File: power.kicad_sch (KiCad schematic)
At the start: 18 parts, among them U2 BQ25176J, U3 TPS61201DRC

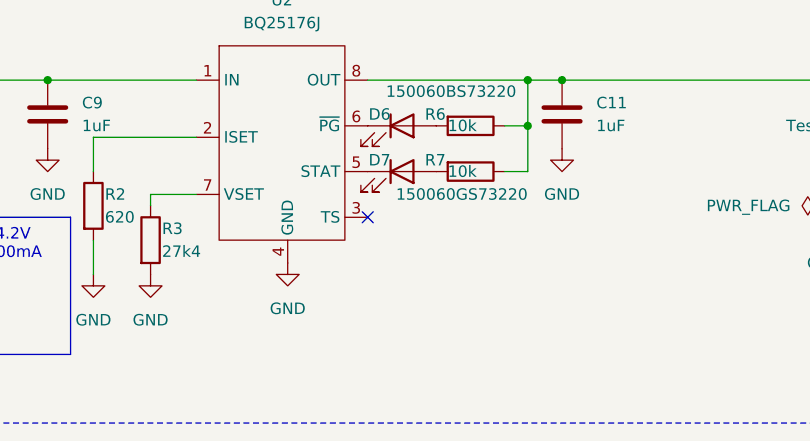
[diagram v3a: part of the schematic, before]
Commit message: fix battery charging IC circuit missing TS pulldown
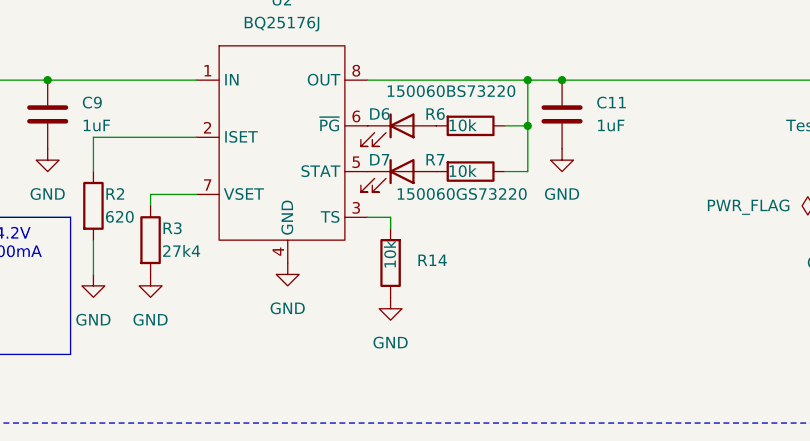
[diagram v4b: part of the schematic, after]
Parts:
- added R14: 10k, Resistor_SMD:R_0805_2012Metric, symbol Device:R
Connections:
- net GND: now also R14.1
- net at U2.3 (TS): now also R14.2
- no-connect marks 1 -> 0
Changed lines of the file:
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@@
 		(color 0 0 0 0)
 	)
-	(no_connect
-		(at 74.93 135.89)
-	)
 	(wire
 		(pts
@@
 	(wire
 		(pts
+			(xy 77.47 137.16) (xy 77.47 135.89)
+		)
+		(stroke
+			(width 0)
+			(type default)
+		)
+	)
+	(wire
+		(pts
 			(xy 68.58 57.15) (xy 80.01 57.15)
 		)
@@
 		(pts
 			(xy 60.96 57.15) (xy 68.58 57.15)
+		)
+		(stroke
+			(width 0)
+			(type default)
+		)
+	)
+	(wire
+		(pts
+			(xy 77.47 135.89) (xy 74.93 135.89)
 		)
 		(stroke
@@
 	)
 	(symbol
+		(lib_id "Device:R")
+		(at 77.47 140.97 180)
+		(unit 1)
+		(exclude_from_sim no)
+		(in_bom yes)
+		(on_board yes)
+		(dnp no)
+		(property "Reference" "R14"
+			(at 83.82 140.716 0)
+			(effects
+				(font
+					(size 1.27 1.27)
+				)
+				(justify left)
+			)
+		)
+		(property "Value" "10k"
+			(at 77.47 138.43 90)
+			(effects
+				(font
+					(size 1.27 1.27)
+				)
+				(justify left)
+			)
+		)
+		(property "Footprint" "Resistor_SMD:R_0805_2012Metric"
+			(at 79.248 140.97 90)
+			(effects
+				(font
+					(size 1.27 1.27)
+				)
+				(hide yes)
+			)
+		)
+		(property "Datasheet" "~"
+			(at 77.47 140.97 0)
+			(effects
+				(font
+					(size 1.27 1.27)
+				)
+				(hide yes)
+			)
+		)
+		(property "Description" "Resistor"
+			(at 77.47 140.97 0)
+			(effects
+				(font
+					(size 1.27 1.27)
+				)
+				(hide yes)
+			)
+		)
+		(property "mpn" "CR0805-FX-1002ELF "
+			(at 77.47 140.97 0)
+			(effects
+				(font
+					(size 1.27 1.27)
+				)
+				(hide yes)
+			)
+		)
+		(pin "1"
+		)
+		(pin "2"
+		)
+		(instances
+			(project "bierdeckel"
+				(path "/a4ffe097-37ef-4e19-a91a-ae57f4a5aad1/06d9cd17-cb19-4cdd-8e67-c41d1b4a676e"
+					(reference "R14")
+					(unit 1)
+				)
+			)
+		)
+	)
+	(symbol
 		(lib_id "power:+3.3V")
 		(at 125.73 59.69 0)
@@
 					(unit 1)
 				)
+			)
+		)
+	)
+	(symbol
+		(lib_id "power:GND")
+		(at 77.47 144.78 0)
+		(unit 1)
+		(exclude_from_sim no)
+		(in_bom yes)
+		(on_board yes)
+		(dnp no)
+		(fields_autoplaced yes)
+		(property "Reference" "#PWR010"
+			(at 77.47 151.13 0)
+			(effects
+				(font
+					(size 1.27 1.27)
+				)
+				(hide yes)
+			)
+		)
+		(property "Value" "GND"
+			(at 77.47 149.86 0)
+			(effects
+				(font
+					(size 1.27 1.27)
+				)
+			)
+		)
+		(property "Footprint" ""
+			(at 77.47 144.78 0)
+			(effects
+				(font
+					(size 1.27 1.27)
+				)
+				(hide yes)
+			)
+		)
+		(property "Datasheet" ""
+			(at 77.47 144.78 0)
+			(effects
+				(font
+					(size 1.27 1.27)
+				)
+				(hide yes)
+			)
+		)
+		(property "Description" "Power symbol creates a global label with name \"GND\" , ground"
+			(at 77.47 144.78 0)
+			(effects
+				(font
+					(size 1.27 1.27)
+				)
+				(hide yes)
+			)
+		)
+		(pin "1"
+		)
+		(instances
+			(project "bierdeckel"
+				(path "/a4ffe097-37ef-4e19-a91a-ae57f4a5aad1/06d9cd17-cb19-4cdd-8e67-c41d1b4a676e"
+					(reference "#PWR010")
+					(unit 1)
+				)

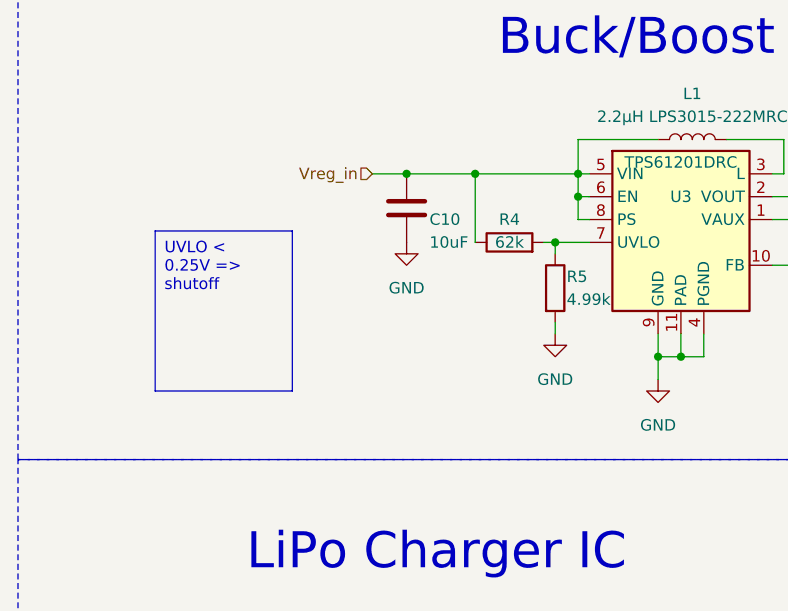
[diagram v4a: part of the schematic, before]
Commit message: correct buck/boost bootstrap circuit to handle falling/rising hysteresis on Uvlo
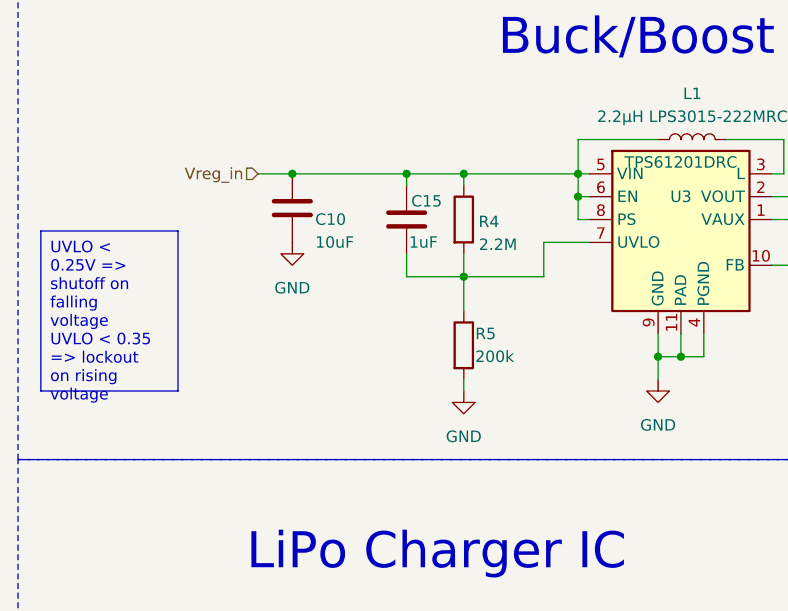
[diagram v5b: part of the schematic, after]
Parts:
- added C15: 1uF, Capacitor_SMD:C_0805_2012Metric, symbol Device:C
- R4: value 62k -> 2.2M
- R5: value 4.99k -> 200k
- U3: footprint Package_SON:Texas_S-PVSON-N10_ThermalVias -> bier:Texas_S-PVSON-N10_ThermalVias; symbol Regulator_Switching:TPS61201DRC -> bier:TPS61201DRC
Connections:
- net Vreg_in: now also C15.1
- net at R4.2, R5.1, U3.7 (UVLO): now also C15.2
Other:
- moved on the sheet: C10, R4, R5

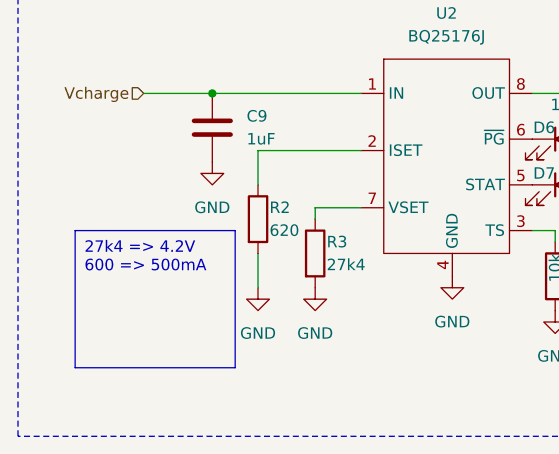
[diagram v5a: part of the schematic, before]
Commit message: change to 2 pressure gauge strips
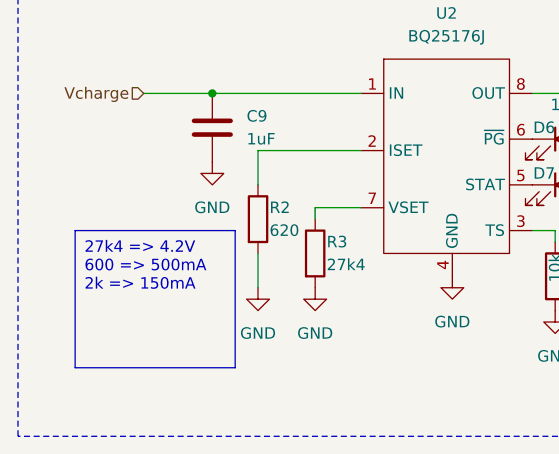
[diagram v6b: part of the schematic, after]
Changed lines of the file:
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@@
 		)
 	)
-	(text_box "27k4 => 4.2V\n600 => 500mA"
+	(text_box "27k4 => 4.2V\n600 => 500mA\n2k => 150mA"
 		(exclude_from_sim no)
 		(at 24.13 135.89 0)

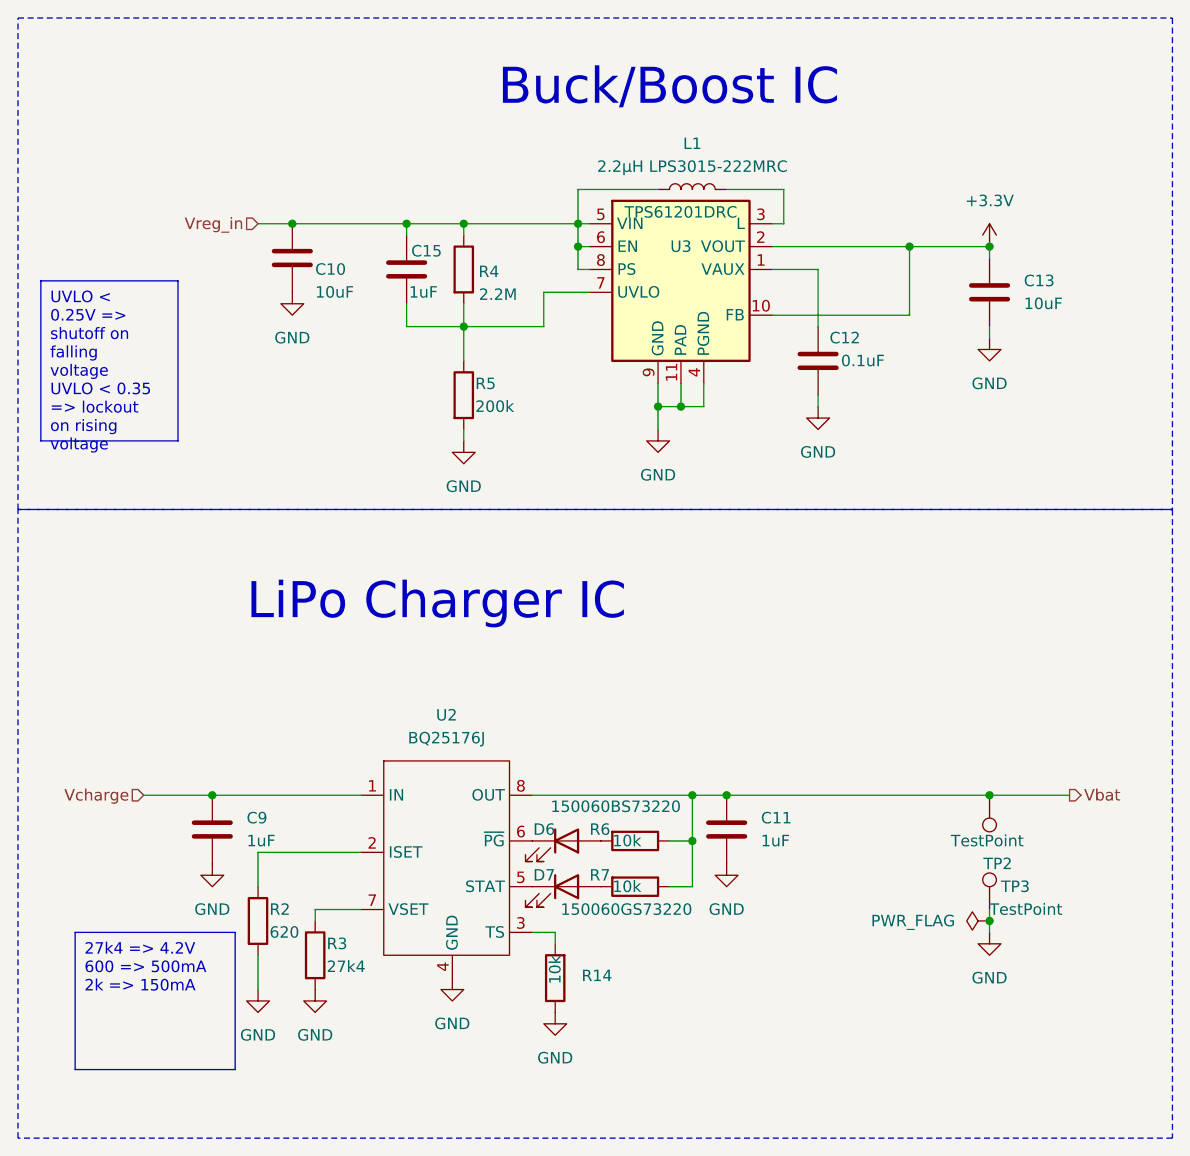
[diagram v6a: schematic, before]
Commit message: reannotate components and move some designators
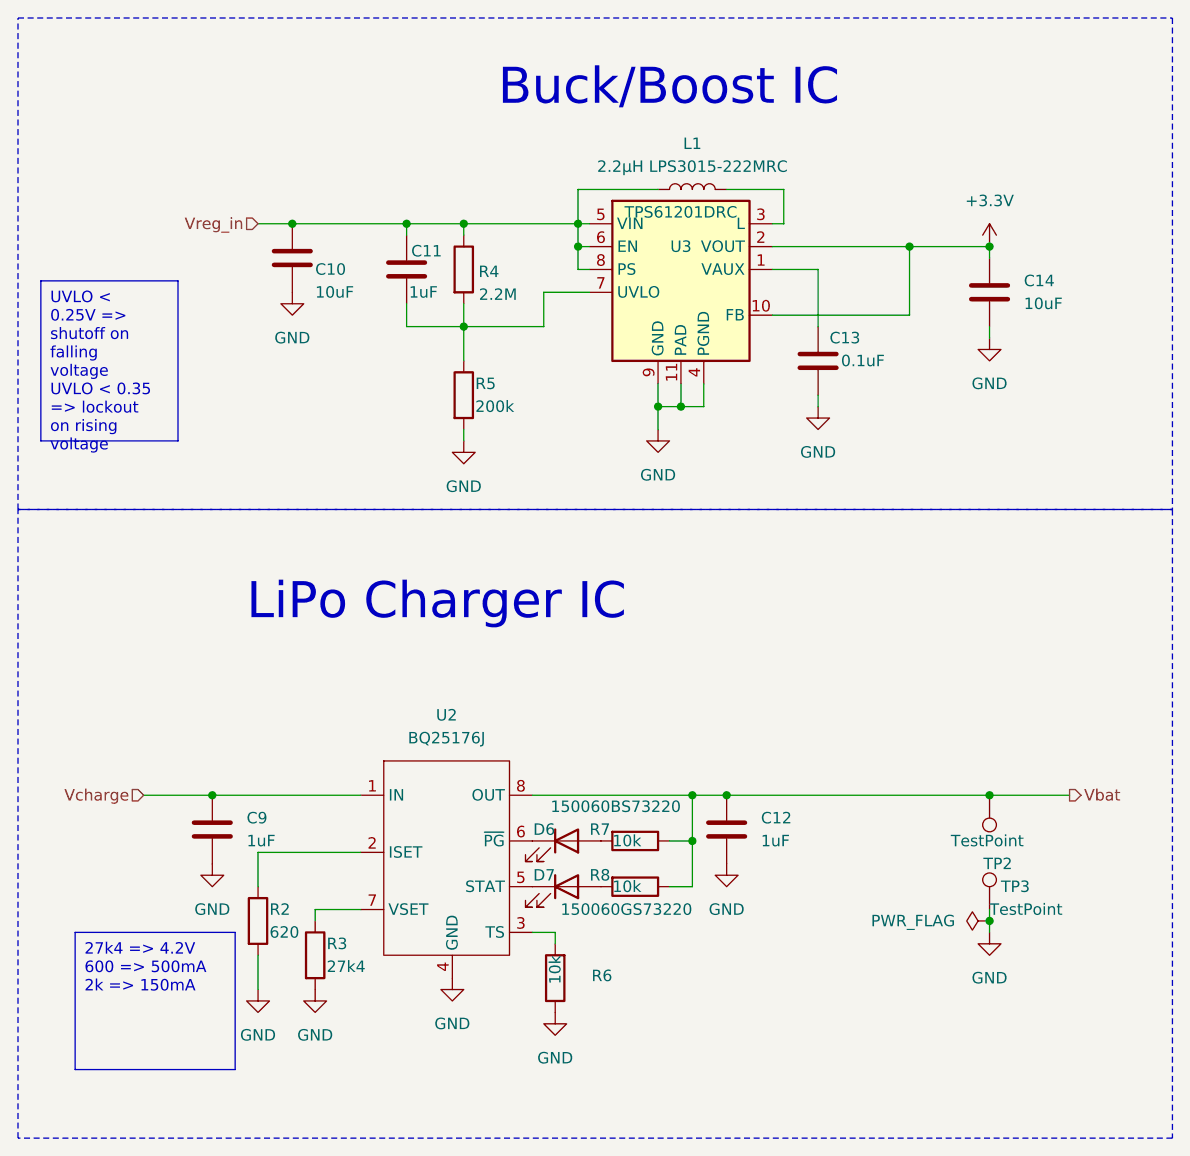
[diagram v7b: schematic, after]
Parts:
- renumbered C15 to C11, C11 to C12, C12 to C13, C13 to C14, R14 to R6, R6 to R7, R7 to R8
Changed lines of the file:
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@@
 		(dnp no)
 		(fields_autoplaced yes)
-		(property "Reference" "#PWR036"
+		(property "Reference" "#PWR033"
 			(at 39.37 134.62 0)
 			(effects
@@
 			(project "bierdeckel"
 				(path "/a4ffe097-37ef-4e19-a91a-ae57f4a5aad1/06d9cd17-cb19-4cdd-8e67-c41d1b4a676e"
-					(reference "#PWR036")
+					(reference "#PWR033")
 					(unit 1)
 				)
@@
 		(dnp no)
 		(fields_autoplaced yes)
-		(property "Reference" "C11"
+		(property "Reference" "C12"
 			(at 100.33 123.19 0)
 			(effects
@@
 			(project "bierdeckel"
 				(path "/a4ffe097-37ef-4e19-a91a-ae57f4a5aad1/06d9cd17-cb19-4cdd-8e67-c41d1b4a676e"
-					(reference "C11")
+					(reference "C12")
 					(unit 1)
 				)
@@
 		(dnp no)
 		(fields_autoplaced yes)
-		(property "Reference" "#PWR037"
+		(property "Reference" "#PWR034"
 			(at 44.45 148.59 0)
 			(effects
@@
 			(project "bierdeckel"
 				(path "/a4ffe097-37ef-4e19-a91a-ae57f4a5aad1/06d9cd17-cb19-4cdd-8e67-c41d1b4a676e"
-					(reference "#PWR037")
+					(reference "#PWR034")
 					(unit 1)
 				)
@@
 		(dnp no)
 		(fields_autoplaced yes)
-		(property "Reference" "#PWR039"
+		(property "Reference" "#PWR035"
 			(at 48.26 71.12 0)
 			(effects
@@
 			(project "bierdeckel"
 				(path "/a4ffe097-37ef-4e19-a91a-ae57f4a5aad1/06d9cd17-cb19-4cdd-8e67-c41d1b4a676e"
-					(reference "#PWR039")
+					(reference "#PWR035")
 					(unit 1)
 				)
@@
 		(dnp no)
 		(fields_autoplaced yes)
-		(property "Reference" "#PWR043"
+		(property "Reference" "#PWR041"
 			(at 96.52 134.62 0)
 			(effects
@@
 			(project "bierdeckel"
 				(path "/a4ffe097-37ef-4e19-a91a-ae57f4a5aad1/06d9cd17-cb19-4cdd-8e67-c41d1b4a676e"
-					(reference "#PWR043")
+					(reference "#PWR041")
 					(unit 1)
 				)
@@
 		(on_board yes)
 		(dnp no)
-		(property "Reference" "C12"
+		(property "Reference" "C13"
 			(at 107.95 69.85 0)
 			(effects
@@
 			(project "bierdeckel"
 				(path "/a4ffe097-37ef-4e19-a91a-ae57f4a5aad1/06d9cd17-cb19-4cdd-8e67-c41d1b4a676e"
-					(reference "C12")
+					(reference "C13")
 					(unit 1)
 				)
@@
 		(dnp no)
 		(fields_autoplaced yes)
-		(property "Reference" "#PWR042"
+		(property "Reference" "#PWR040"
 			(at 88.9 86.36 0)
 			(effects
@@
 			(project "bierdeckel"
 				(path "/a4ffe097-37ef-4e19-a91a-ae57f4a5aad1/06d9cd17-cb19-4cdd-8e67-c41d1b4a676e"
-					(reference "#PWR042")
+					(reference "#PWR040")
 					(unit 1)
 				)
@@
 		(on_board yes)
 		(dnp no)
-		(property "Reference" "C15"
+		(property "Reference" "C11"
 			(at 61.468 60.198 0)
 			(effects
@@
 			(project "bierdeckel"
 				(path "/a4ffe097-37ef-4e19-a91a-ae57f4a5aad1/06d9cd17-cb19-4cdd-8e67-c41d1b4a676e"
-					(reference "C15")
+					(reference "C11")
 					(unit 1)
 				)
@@
 		(on_board yes)
 		(dnp no)
-		(property "Reference" "R7"
+		(property "Reference" "R8"
 			(at 81.28 129.54 90)
 			(effects
@@
 			(project "bierdeckel"
 				(path "/a4ffe097-37ef-4e19-a91a-ae57f4a5aad1/06d9cd17-cb19-4cdd-8e67-c41d1b4a676e"
-					(reference "R7")
+					(reference "R8")
 					(unit 1)
 				)
@@
 		(dnp no)
 		(fields_autoplaced yes)
-		(property "Reference" "C13"
+		(property "Reference" "C14"
 			(at 129.54 63.5 0)
 			(effects
@@
 			(project "bierdeckel"
 				(path "/a4ffe097-37ef-4e19-a91a-ae57f4a5aad1/06d9cd17-cb19-4cdd-8e67-c41d1b4a676e"
-					(reference "C13")
+					(reference "C14")
 					(unit 1)
 				)
@@
 		(dnp no)
 		(fields_autoplaced yes)
-		(property "Reference" "#PWR046"
+		(property "Reference" "#PWR044"
 			(at 125.73 76.2 0)
 			(effects
@@
 			(project "bierdeckel"
 				(path "/a4ffe097-37ef-4e19-a91a-ae57f4a5aad1/06d9cd17-cb19-4cdd-8e67-c41d1b4a676e"
-					(reference "#PWR046")
+					(reference "#PWR044")
 					(unit 1)
 				)
@@
 		(dnp no)
 		(fields_autoplaced yes)
-		(property "Reference" "#PWR041"
+		(property "Reference" "#PWR038"
 			(at 67.31 87.63 0)
 			(effects
@@
 			(project "bierdeckel"
 				(path "/a4ffe097-37ef-4e19-a91a-ae57f4a5aad1/06d9cd17-cb19-4cdd-8e67-c41d1b4a676e"
-					(reference "#PWR041")
+					(reference "#PWR038")
 					(unit 1)
 				)
@@
 		(on_board yes)
 		(dnp no)
-		(property "Reference" "R14"
+		(property "Reference" "R6"
 			(at 83.82 140.716 0)
 			(effects
@@
 			(project "bierdeckel"
 				(path "/a4ffe097-37ef-4e19-a91a-ae57f4a5aad1/06d9cd17-cb19-4cdd-8e67-c41d1b4a676e"
-					(reference "R14")
+					(reference "R6")
 					(unit 1)
 				)
@@
 		(dnp no)
 		(fields_autoplaced yes)
-		(property "Reference" "#PWR045"
+		(property "Reference" "#PWR043"
 			(at 125.73 63.5 0)
 			(effects
@@
 			(project "bierdeckel"
 				(path "/a4ffe097-37ef-4e19-a91a-ae57f4a5aad1/06d9cd17-cb19-4cdd-8e67-c41d1b4a676e"
-					(reference "#PWR045")
+					(reference "#PWR043")
 					(unit 1)
 				)
@@
 		(dnp no)
 		(fields_autoplaced yes)
-		(property "Reference" "#PWR040"
+		(property "Reference" "#PWR037"
 			(at 66.04 147.32 0)
 			(effects
@@
 			(project "bierdeckel"
 				(path "/a4ffe097-37ef-4e19-a91a-ae57f4a5aad1/06d9cd17-cb19-4cdd-8e67-c41d1b4a676e"
-					(reference "#PWR040")
+					(reference "#PWR037")
 					(unit 1)
 				)
@@
 		(dnp no)
 		(fields_autoplaced yes)
-		(property "Reference" "#PWR038"
+		(property "Reference" "#PWR036"
 			(at 50.8 148.59 0)
 			(effects
@@
 			(project "bierdeckel"
 				(path "/a4ffe097-37ef-4e19-a91a-ae57f4a5aad1/06d9cd17-cb19-4cdd-8e67-c41d1b4a676e"
-					(reference "#PWR038")
+					(reference "#PWR036")
 					(unit 1)
 				)
@@
 		(on_board yes)
 		(dnp no)
-		(property "Reference" "R6"
+		(property "Reference" "R7"
 			(at 81.28 124.46 90)
 			(effects
@@
 			(project "bierdeckel"
 				(path "/a4ffe097-37ef-4e19-a91a-ae57f4a5aad1/06d9cd17-cb19-4cdd-8e67-c41d1b4a676e"
-					(reference "R6")
+					(reference "R7")
 					(unit 1)
 				)
@@
 		(dnp no)
 		(fields_autoplaced yes)
-		(property "Reference" "#PWR044"
+		(property "Reference" "#PWR042"
 			(at 106.68 83.82 0)
 			(effects
@@
 			(project "bierdeckel"
 				(path "/a4ffe097-37ef-4e19-a91a-ae57f4a5aad1/06d9cd17-cb19-4cdd-8e67-c41d1b4a676e"
-					(reference "#PWR044")
+					(reference "#PWR042")
 					(unit 1)
 				)
@@
 		(dnp no)
 		(fields_autoplaced yes)
-		(property "Reference" "#PWR047"
+		(property "Reference" "#PWR045"
 			(at 125.73 142.24 0)
 			(effects
@@
 			(project "bierdeckel"
 				(path "/a4ffe097-37ef-4e19-a91a-ae57f4a5aad1/06d9cd17-cb19-4cdd-8e67-c41d1b4a676e"
-					(reference "#PWR047")
+					(reference "#PWR045")
 					(unit 1)
 				)
@@
 		(dnp no)
 		(fields_autoplaced yes)
-		(property "Reference" "#PWR010"
+		(property "Reference" "#PWR039"
 			(at 77.47 151.13 0)
 			(effects
@@
 			(project "bierdeckel"
 				(path "/a4ffe097-37ef-4e19-a91a-ae57f4a5aad1/06d9cd17-cb19-4cdd-8e67-c41d1b4a676e"
-					(reference "#PWR010")
-					(unit 1)
-				)
+					(reference "#PWR039")
+					(unit 1)
+				)
